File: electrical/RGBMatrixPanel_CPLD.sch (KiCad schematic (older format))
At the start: 29 parts, among them J1 CONN_01X04, J2 CONN_01X04, J3 CONN_01X04, J4 CONN_02X06, J5 CONN_02X08, J6 CONN_01X04, J7 BARREL_JACK, J8 CONN_01X08, J9 CONN_02X06, Q1 Photo_Trans, U1 PHOTON, U2 LC4032V-44TQFP, U3 TSOP75238TT, X1 MTHOLE, X2 MTHOLE, X3 MTHOLE, X4 MTHOLE

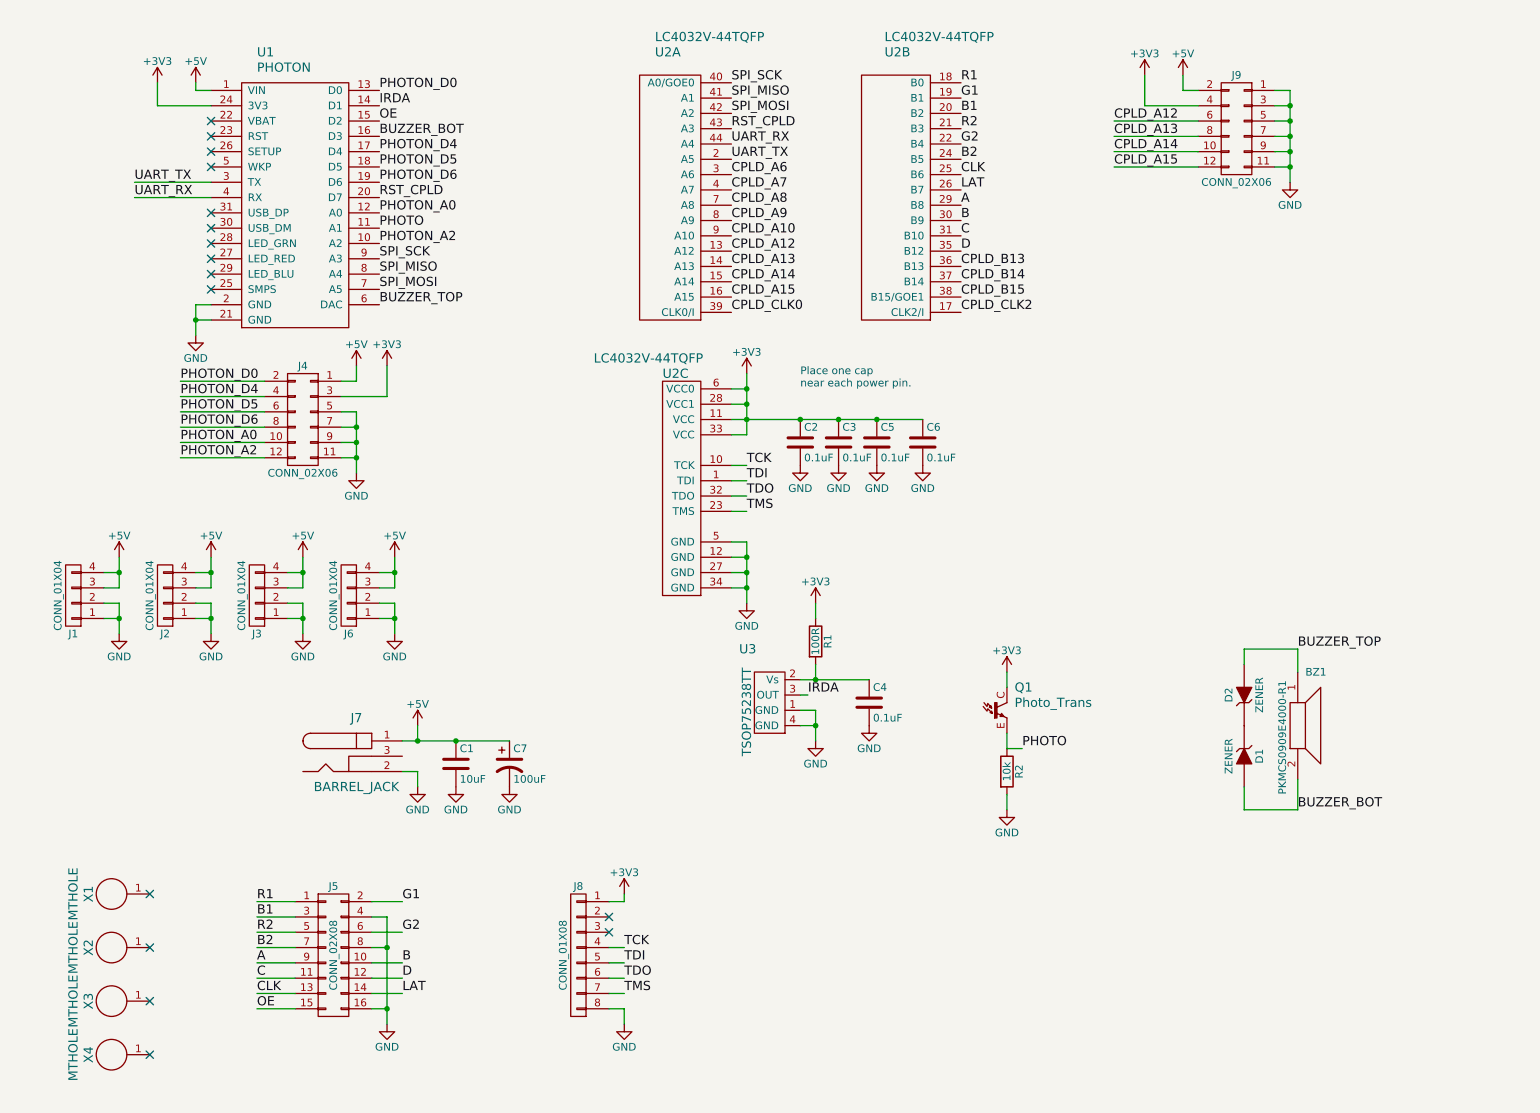
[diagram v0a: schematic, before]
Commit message: Rev 2
Updated board to Rev 2. Removed buzzer. Reduced number spare GPIOs.
Added HW to program CPLD from Photon. Updated CPLD pinout in Lattice SW.
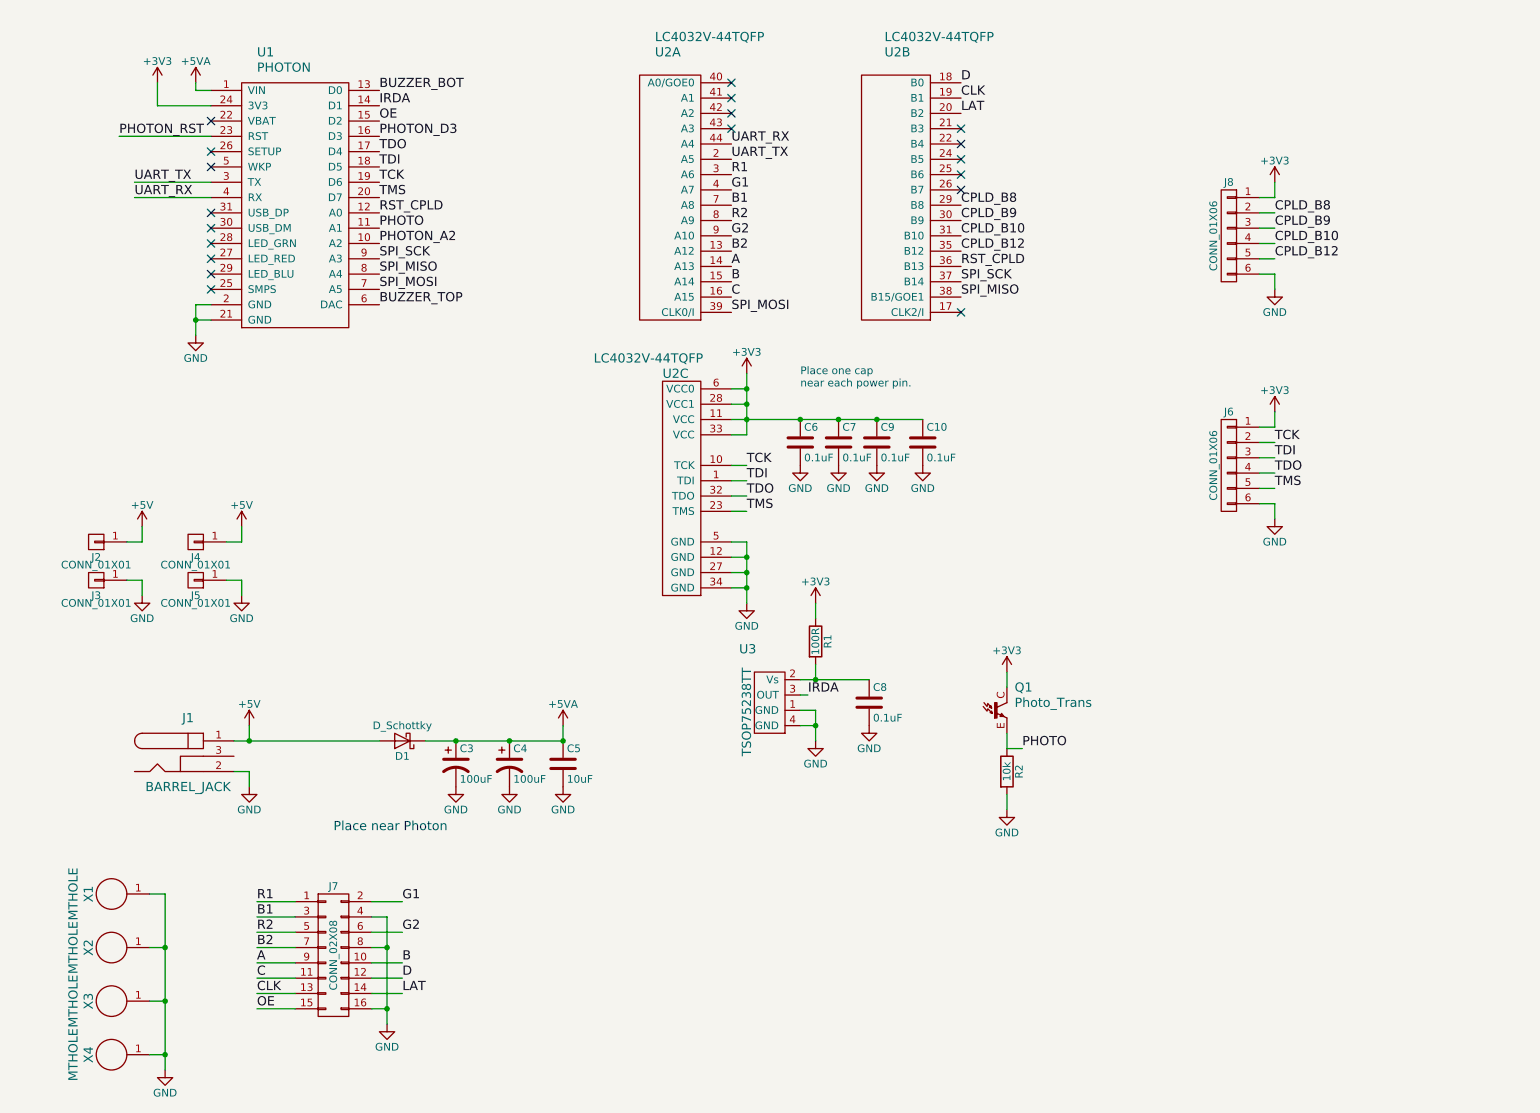
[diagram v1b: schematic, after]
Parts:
- removed BZ1: PKMCS0909E4000-R1, Jason_Libraries:PKMCS0909E4000-R1, symbol PKMCS0909E4000-R1
- removed C1: 10uF, Capacitors_SMD:C_0805, symbol C
- removed C7: 100uF, Jason_Libraries:c_elec_6.3x7.7, symbol CP1
- removed D1, D2: ZENER, Diodes_SMD:SOD-123, symbol ZENER
- removed J1, J2, J3, J6: CONN_01X04, Jason_Libraries:VH_THRU_01x04_RA, symbol CONN_01X04
- removed J4, J9: CONN_02X06, Jason_Libraries:HEADER_THRU_02x06, symbol CONN_02X06
- removed J8: CONN_01X08, Jason_Libraries:HEADER_THRU_01x08, symbol CONN_01X08
- added C3, C4: 100uF, Capacitors_SMD:c_elec_6.3x5.7, symbol CP1
- added C5: 10uF, Capacitors_SMD:C_0805, symbol C
- added D1: D_Schottky, Reclaimer_Labs:SMini2-F5-B, symbol D_Schottky
- added J2, J3, J4, J5: CONN_01X01, Reclaimer_Labs:3547, symbol CONN_01X01
- added J6, J8: CONN_01X06, Socket_Strips:Socket_Strip_Straight_1x06, symbol CONN_01X06
- J1: renamed from J7; footprint Connect:BARREL_JACK -> Reclaimer_Labs:BARREL_JACK_MPD_EJ508A
- J7: renamed from J5; footprint Jason_Libraries:HEADER_THRU_02x08_POL -> Reclaimer_Labs:HEADER_THRU_02x08_POL
- Q1: footprint Jason_Libraries:Photo_Trans_0805 -> Reclaimer_Labs:Photo_Trans_0805
- U1: footprint Jason_Libraries:PHOTON -> Reclaimer_Labs:PHOTON
- U2: footprint Jason_Libraries:QFP_44 -> Reclaimer_Labs:QFP_44
- U3: footprint Jason_Libraries:TSOP75238TT -> Reclaimer_Labs:TSOP75238TT
- X1, X2: footprint Mounting_Holes:MountingHole_3-5mm -> Mounting_Holes:MountingHole_3.5mm
- X3, X4: footprint Mounting_Holes:MountingHole_3-5mm -> Reclaimer_Labs:MountingHole_3.5mm_Pad_Via
- renumbered C6 to C10, C2 to C6, C3 to C7, C4 to C8, C5 to C9
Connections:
- net CPLD_A10 is gone; now on net G2: U2.9 (A10)
- net CPLD_A12 is gone; now on net B2: U2.13 (A12)
- net CPLD_A13 is gone; now on net A: U2.14 (A13)
- net CPLD_A14 is gone; now on net B: U2.15 (A14)
- net CPLD_A15 is gone; now on net C: U2.16 (A15)
- net CPLD_A6 is gone; now on net R1: U2.3 (A6)
- net CPLD_A7 is gone; now on net G1: U2.4 (A7)
- net CPLD_A8 is gone; now on net B1: U2.7 (A8)
- net CPLD_A9 is gone; now on net R2: U2.8 (A9)
- net CPLD_B13 is gone; now on net RST_CPLD: U2.36 (B13)
- net CPLD_B14 is gone; now on net SPI_SCK: U2.37 (B14)
- net CPLD_B15 is gone; now on net SPI_MISO: U2.38 (B15/GOE1)
- net CPLD_CLK0 is gone; now on net SPI_MOSI: U2.39 (CLK0/I)
- net PHOTON_A0 is gone; now on net RST_CPLD: U1.12 (A0)
- net PHOTON_D0 is gone; now on net BUZZER_BOT: U1.13 (D0)
- net PHOTON_D4 is gone; now on net TDO: U1.17 (D4)
- net PHOTON_D5 is gone; now on net TDI: U1.18 (D5)
- net PHOTON_D6 is gone; now on net TCK: U1.19 (D6)
- net +3V3: now also J6.1 (P1), J8.1 (P1)
- net +5V: now also D1.2 (A), J2.1 (P1), J4.1 (P1); no longer U1.1 (VIN)
- net A: no longer U2.29 (B8)
- net B: no longer U2.30 (B9)
- net B1: no longer U2.20 (B2)
- net B2: no longer U2.24 (B5)
- net BUZZER_BOT: no longer U1.16 (D3)
- net C: no longer U2.31 (B10)
- net CLK: now also U2.19 (B1); no longer U2.25 (B6)
- net D: now also U2.18 (B0); no longer U2.35 (B12)
- net G1: no longer U2.19 (B1)
- net G2: no longer U2.22 (B4)
- net GND: now also X1.1, X2.1, X3.1, X4.1, C3.2, C4.2, C5.2, J3.1 (P1), J5.1 (P1), J6.6 (P6), J8.6 (P6)
- net LAT: now also U2.20 (B2); no longer U2.26 (B7)
- net R1: no longer U2.18 (B0)
- net R2: no longer U2.21 (B3)
- net RST_CPLD: no longer U1.20 (D7), U2.43 (A3)
- net SPI_MISO: no longer U2.41 (A1)
- net SPI_MOSI: no longer U2.42 (A2)
- net SPI_SCK: no longer U2.40 (A0/GOE0)
- net TCK: now also J6.2 (P2)
- net TDI: now also J6.3 (P3)
- net TDO: now also J6.4 (P4)
- net TMS: now also U1.20 (D7), J6.5 (P5)
- net PHOTON_RST: now reaches U1.23 (RST)
- net CPLD_CLK2: no longer names the net of U2.17 (CLK2/I)
- new net +5VA: C3.1, C4.1, C5.1, D1.1 (K), U1.1 (VIN)
- new net CPLD_B10: J8.4 (P4), U2.31 (B10)
- new net CPLD_B12: J8.5 (P5), U2.35 (B12)
- new net CPLD_B8: J8.2 (P2), U2.29 (B8)
- new net CPLD_B9: J8.3 (P3), U2.30 (B9)
- new net PHOTON_D3: U1.16 (D3)
- no-connect marks 16 -> 19
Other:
- note added: "Place near Photon"
- moved on the sheet: J1

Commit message: Rev 3
Updates include new board outline to accomendate mounting to sheet metal
frame
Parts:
- removed X4: MTHOLE, Reclaimer_Labs:MountingHole_3.5mm_Pad_Via, symbol MTHOLE
- C5: footprint Capacitors_SMD:C_0805 -> Capacitors_SMD:C_1206
- D1: footprint Reclaimer_Labs:SMini2-F5-B -> Reclaimer_Labs:SMA
- J1: footprint Reclaimer_Labs:BARREL_JACK_MPD_EJ508A -> Reclaimer_Labs:BARREL_JACK_PJ_202AH_Slots
- U3: value TSOP75238TT -> TSSP77P38TTR; Manufacturer Part Number TSOP75238TR -> TSSP77P38TT; Supplier 1 Part Number TSOP75238CT-ND -> TSSP77P38TTR-ND
- X1, X2: footprint Mounting_Holes:MountingHole_3.5mm -> Reclaimer_Labs:MountingHole_3.5mm_Pad_Via
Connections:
- net UART_RX: no longer U2.44 (A4)
- net UART_TX: no longer U2.2 (A5)
- no-connect marks 19 -> 21
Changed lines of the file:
@@
 P 5600 5050
 F 0 "U3" H 5300 5400 60  0000 L CNN
-F 1 "TSOP75238TT" V 5350 4700 60  0000 L CNN
+F 1 "TSSP77P38TTR" V 5350 4700 60  0000 L CNN
 F 2 "Reclaimer_Labs:TSOP75238TT" H 5600 5200 60  0001 C CNN
 F 3 "" H 5600 5200 60  0000 C CNN
 F 4 "Vishay" H 5600 5050 60  0001 C CNN "Manufacturer"
-F 5 "TSOP75238TR" H 5600 5050 60  0001 C CNN "Manufacturer Part Number"
+F 5 "TSSP77P38TT" H 5600 5050 60  0001 C CNN "Manufacturer Part Number"
 F 6 "Digikey" H 5600 5050 60  0001 C CNN "Supplier 1"
-F 7 "TSOP75238CT-ND" H 5600 5050 60  0001 C CNN "Supplier 1 Part Number"
+F 7 "TSSP77P38TTR-ND" H 5600 5050 60  0001 C CNN "Supplier 1 Part Number"
 	1    5600 5050
 	1    0    0    -1
@@
 F 0 "J1" H 1700 5650 60  0000 C CNN
 F 1 "BARREL_JACK" H 1700 5200 60  0000 C CNN
-F 2 "Reclaimer_Labs:BARREL_JACK_MPD_EJ508A" H 1700 5400 60  0001 C CNN
+F 2 "Reclaimer_Labs:BARREL_JACK_PJ_202AH_Slots" H 1700 5400 60  0001 C CNN
 F 3 "" H 1700 5400 60  0000 C CNN
 F 4 "CUI" H 1700 5400 60  0001 C CNN "Manufacturer"
@@
 Text Label 1350 1650 0    60   ~ 0
 UART_TX
-Text Label 5250 1500 0    60   ~ 0
-UART_TX
-Text Label 5250 1400 0    60   ~ 0
-UART_RX
 NoConn ~ 1850 1850
 NoConn ~ 1850 1950
@@
 F 0 "X1" H 1200 6450 60  0000 C CNN
 F 1 "MTHOLE" H 1200 6550 60  0000 C CNN
-F 2 "Mounting_Holes:MountingHole_3.5mm" H 1200 6300 60  0001 C CNN
+F 2 "Reclaimer_Labs:MountingHole_3.5mm_Pad_Via" H 1200 6300 60  0001 C CNN
 F 3 "" H 1200 6300 60  0000 C CNN
 	1    1200 6300
@@
 F 0 "X2" H 1200 6800 60  0000 C CNN
 F 1 "MTHOLE" H 1200 6900 60  0000 C CNN
-F 2 "Mounting_Holes:MountingHole_3.5mm" H 1200 6650 60  0001 C CNN
+F 2 "Reclaimer_Labs:MountingHole_3.5mm_Pad_Via" H 1200 6650 60  0001 C CNN
 F 3 "" H 1200 6650 60  0000 C CNN
 	1    1200 6650
@@
 F 0 "D1" H 3100 5400 50  0000 C CNN
 F 1 "D_Schottky" H 3100 5200 50  0000 C CNN
-F 2 "Reclaimer_Labs:SMini2-F5-B" H 3100 5300 50  0001 C CNN
+F 2 "Reclaimer_Labs:SMA" H 3100 5300 50  0001 C CNN
 F 3 "" H 3100 5300 50  0000 C CNN
 F 4 "Panasonic" H 3100 5300 60  0001 C CNN "Manufacturer"
@@
 F 0 "C5" H 4175 5550 50  0000 L CNN
 F 1 "10uF" H 4175 5350 50  0000 L CNN
-F 2 "Capacitors_SMD:C_0805" H 4188 5300 30  0001 C CNN
+F 2 "Capacitors_SMD:C_1206" H 4188 5300 30  0001 C CNN
 F 3 "" H 4150 5450 60  0000 C CNN
 F 4 "Yageo" H 4150 5450 60  0001 C CNN "Manufacturer"
@@
 	1550 6300 1550 7450
 Wire Wire Line
-	1550 7350 1450 7350
-Wire Wire Line
 	1450 7000 1550 7000
-Connection ~ 1550 7350
 Wire Wire Line
 	1450 6650 1550 6650
@@
 NoConn ~ 6750 1400
 NoConn ~ 6750 2500
-$Comp
-L MTHOLE X4
-U 1 1 565391B6
-P 1200 7350
-F 0 "X4" H 1200 7500 60  0000 C CNN
-F 1 "MTHOLE" H 1200 7600 60  0000 C CNN
-F 2 "Reclaimer_Labs:MountingHole_3.5mm_Pad_Via" H 1200 7350 60  0001 C CNN
-F 3 "" H 1200 7350 60  0000 C CNN
-	1    1200 7350
-	0    -1   -1   0
-$EndComp
+NoConn ~ 5250 1400
+NoConn ~ 5250 1500
 $EndSCHEMATC

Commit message: Rev 5
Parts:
- removed C3, C4: 100uF, Capacitors_SMD:c_elec_6.3x5.7, symbol CP1
- removed D1: D_Schottky, Reclaimer_Labs:SMA, symbol D_Schottky
- removed U3: TSSP77P38TTR, Reclaimer_Labs:TSOP75238TT, symbol TSOP75238TT
- added C1, C2, C3: 4.7uF, Capacitors_SMD:C_1206, symbol C
- added C11: 0.47uF, Capacitors_SMD:C_0805, symbol C
- added C12: 1.0uF, Capacitors_SMD:C_0603, symbol C
- added C13: 390pF, Capacitors_SMD:C_0603, symbol C
- added C14: 100uF, Capacitors_SMD:C_1206, symbol C
- added C15: DNP, Capacitors_SMD:C_1206, symbol C
- added C4: 0.1uF, Capacitors_SMD:C_0805, symbol C
- added J9: CONN_01X03, Socket_Strips:Socket_Strip_Straight_1x03, symbol CONN_01X03
- added L1: 2.2uH, Reclaimer_Labs:SRR1270, symbol INDUCTOR
- added Q2: CSD17307Q5A, Reclaimer_Labs:MOSFET_Q5A, symbol Q_NMOS_SGD
- added Q3: CSD18531Q5A, Reclaimer_Labs:MOSFET_Q5A, symbol Q_NMOS_SGD
- added R3, R5: 73k2, Capacitors_SMD:C_0603, symbol R
- added R4: 1k69, Capacitors_SMD:C_0603, symbol R
- added R6: 10k, Capacitors_SMD:C_0603, symbol R
- added U3: LM3150, Reclaimer_Labs:TSSOP-14-0.65mm-EP, symbol LM3150
- C5: value 10uF -> 0.01uF; footprint Capacitors_SMD:C_1206 -> Capacitors_SMD:C_0603; MacroFab Part Number (none) -> MF-CAP-0603-0.01uF; Manufacturer Yageo -> (none); Manufacturer Part Number CC0805KKX5R6BB106 -> (none); Supplier 1 Digikey -> (none); Supplier 1 Part Number 311-1460-1-ND -> (none)
- R1, R2: footprint Resistors_SMD:R_0603 -> Capacitors_SMD:C_0603
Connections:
- net PHOTON_A2 is gone; now on net TDO: U1.10 (A2)
- net PHOTON_D3 is gone; now on net TMS: U1.16 (D3)
- net +5V: now also U1.1 (VIN), C13.1, C14.1, C15.1, L1.2, R5.1; no longer J1.1
- net A: now also U2.21 (B3); no longer U2.14 (A13)
- net B: now also U2.22 (B4); no longer U2.15 (A14)
- net B1: now also U2.29 (B8); no longer U2.7 (A8)
- net B2: now also U2.24 (B5); no longer U2.13 (A12)
- net C: now also U2.19 (B1); no longer U2.16 (A15)
- net CLK: now also U2.16 (A15); no longer U2.19 (B1)
- net D: now also U2.20 (B2); no longer U2.18 (B0)
- net G1: now also U2.31 (B10); no longer U2.4 (A7)
- net G2: now also U2.26 (B7); no longer U2.9 (A10)
- net GND: now also C1.2, C12.2, C14.2, C15.2, C2.2, C3.2, C4.2, J9.2 (P2), Q3.1 (S), R6.2, U3.14 (PGND), U3.15 (SGND), U3.5 (SGND), U3.9 (SGND)
- net IRDA: now also J9.1 (P1)
- net LAT: now also U2.18 (B0); no longer U2.20 (B2)
- net R1: now also U2.30 (B9); no longer U2.3 (A6)
- net R2: now also U2.25 (B6); no longer U2.8 (A9)
- net TDO: no longer U1.17 (D4)
- net TMS: no longer U1.20 (D7)
- net CPLD_A0: now reaches U2.40 (A0/GOE0)
- net CPLD_A0: now also J8.5 (P5)
- net CPLD_A1: now reaches U2.41 (A1)
- net CPLD_A1: now also J8.4 (P4)
- net CPLD_A2: now reaches U2.42 (A2)
- net CPLD_A2: now also J8.3 (P3)
- net CPLD_A3: now reaches U2.43 (A3)
- net CPLD_A3: now also J8.2 (P2)
- net IR_PWR: now reaches C8.1, R1.2
- net IR_PWR: now also J9.3 (P3)
- net +5VA renamed SS
- net SS: now also U3.6 (SS); no longer U1.1 (VIN)
- net BUZZER_BOT: no longer names the net of U1.13 (D0)
- net BUZZER_TOP: no longer names the net of U1.6 (DAC)
- removed net CPLD_B10: J8.4 (P4), U2.31 (B10)
- net CPLD_B12: no longer names the net of U2.35 (B12)
- net CPLD_B12: no longer J8.5 (P5)
- removed net CPLD_B8: J8.2 (P2), U2.29 (B8)
- removed net CPLD_B9: J8.3 (P3), U2.30 (B9)
- new net BST: C11.1, U3.12 (BST)
- new net FB: C13.2, R5.2, R6.1, U3.4 (FB)
- new net HG: Q2.2 (G), U3.11 (HG)
- new net ILIM: R4.2, U3.8 (ILIM)
- new net LG: Q3.2 (G), U3.13 (LG)
- new net RON: R3.2, U3.7 (RON)
- new net SW: C11.2, L1.1, Q2.1 (S), Q3.3 (D), R4.1, U3.10 (SW)
- new net VCC: C12.1, U3.1 (VCC)
- new net VIN: C1.1, C2.1, C3.1, C4.1, J1.1, Q2.3 (D), R3.1, U3.2 (VIN)
- no-connect marks 21 -> 27
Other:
- note removed: "Place near Photon"
- moved on the sheet: C10, C6, C7, C8, C9, J1, J2, J3, J4, J5, J6, J7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
